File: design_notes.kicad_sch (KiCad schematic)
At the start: 0 parts

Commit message: [feat] Add I2C breakout
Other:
- note added: "TODO: - Integrate external power input other than USB power - GPIO breakout - LED where necessary? - I2C breakout"
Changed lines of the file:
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@@
 	(generator_version "10.0")
 	(paper "A4")
+	(text "TODO:\n- Integrate external power input other than USB power\n- GPIO breakout\n- LED where necessary?\n- I2C breakout"
+		(exclude_from_sim no)
+		(at 16.51 125.73 0)
+		(effects
+			(font
+				(size 1.27 1.27)
+			)
+			(justify left)
+		)
+	)
 )

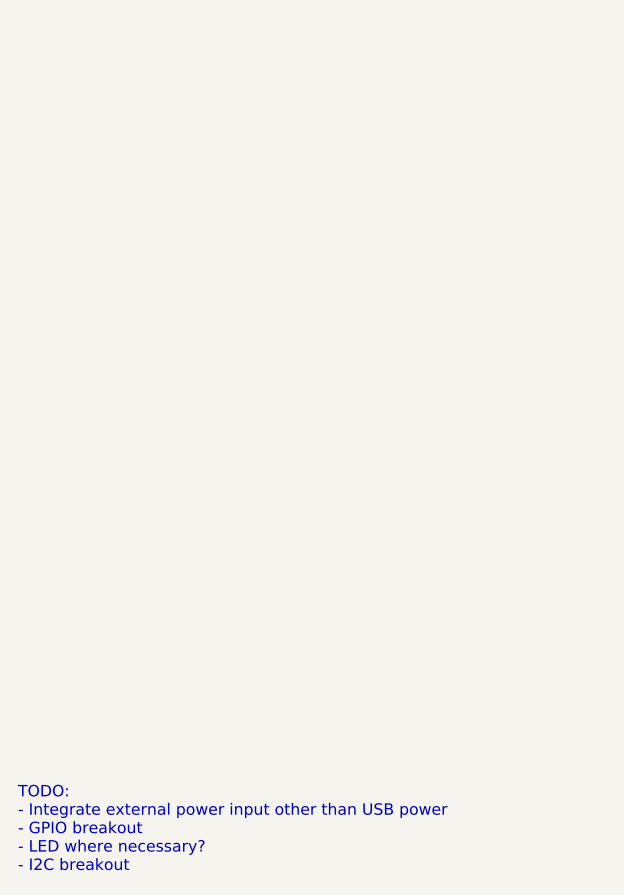
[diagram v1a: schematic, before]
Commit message: [feat] Add OLED I2C breakout for display, Add general purpose GPIOs
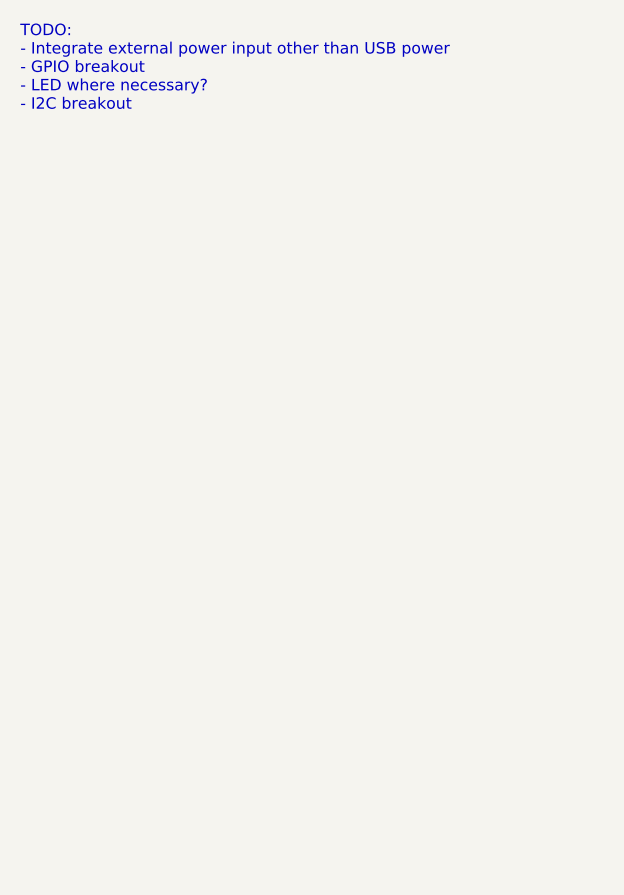
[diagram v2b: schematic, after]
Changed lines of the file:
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@@
 	(text "TODO:\n- Integrate external power input other than USB power\n- GPIO breakout\n- LED where necessary?\n- I2C breakout"
 		(exclude_from_sim no)
-		(at 16.51 125.73 0)
+		(at 16.764 41.148 0)
 		(effects
 			(font
@@
 		)
 	)
+	(sheet_instances
+		(path "/"
+			(page "5")
+		)
+	)

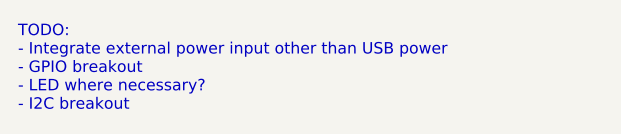
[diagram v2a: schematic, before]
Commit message: [refactor] Remove GPIO12 and GPIO13 for LED green and blue
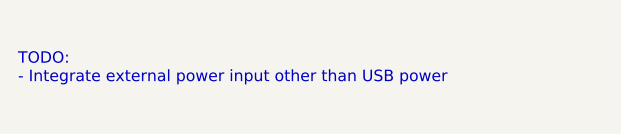
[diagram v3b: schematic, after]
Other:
- note added: "TODO: - Integrate external power input other than USB power"
- note removed: "TODO: - Integrate external power input other than USB power - GPIO breakout - LED where necessary? - I2C breakout"
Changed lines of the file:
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@@
 	(generator_version "10.0")
 	(paper "A4")
-	(text "TODO:\n- Integrate external power input other than USB power\n- GPIO breakout\n- LED where necessary?\n- I2C breakout"
+	(text "TODO:\n- Integrate external power input other than USB power"
 		(exclude_from_sim no)
 		(at 16.764 41.148 0)

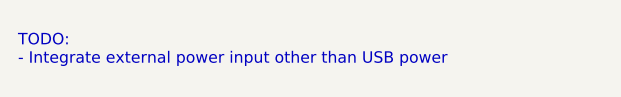
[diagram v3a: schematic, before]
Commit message: [feat] Integrate external battery
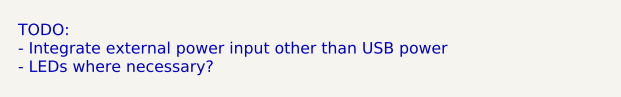
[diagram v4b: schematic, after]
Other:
- note added: "TODO: - Integrate external power input other than USB power - LEDs where necessary?"
- note removed: "TODO: - Integrate external power input other than USB power"
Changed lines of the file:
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@@
 	(generator_version "10.0")
 	(paper "A4")
-	(text "TODO:\n- Integrate external power input other than USB power"
+	(text "TODO:\n- Integrate external power input other than USB power\n- LEDs where necessary?"
 		(exclude_from_sim no)
 		(at 16.764 41.148 0)
@@
 	(sheet_instances
 		(path "/"
-			(page "5")
+			(page "6")
 		)
 	)
